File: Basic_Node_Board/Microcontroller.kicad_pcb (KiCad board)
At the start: 4 copper layers, 100 x 100 mm, 31 parts, among them J1 Conn_01x02, J4 Conn_01x02_Pin, U2 ESP32-DEVKIT-C, U3 TPS54560BQDDARQ1, U6 TJA1050T/CM,118

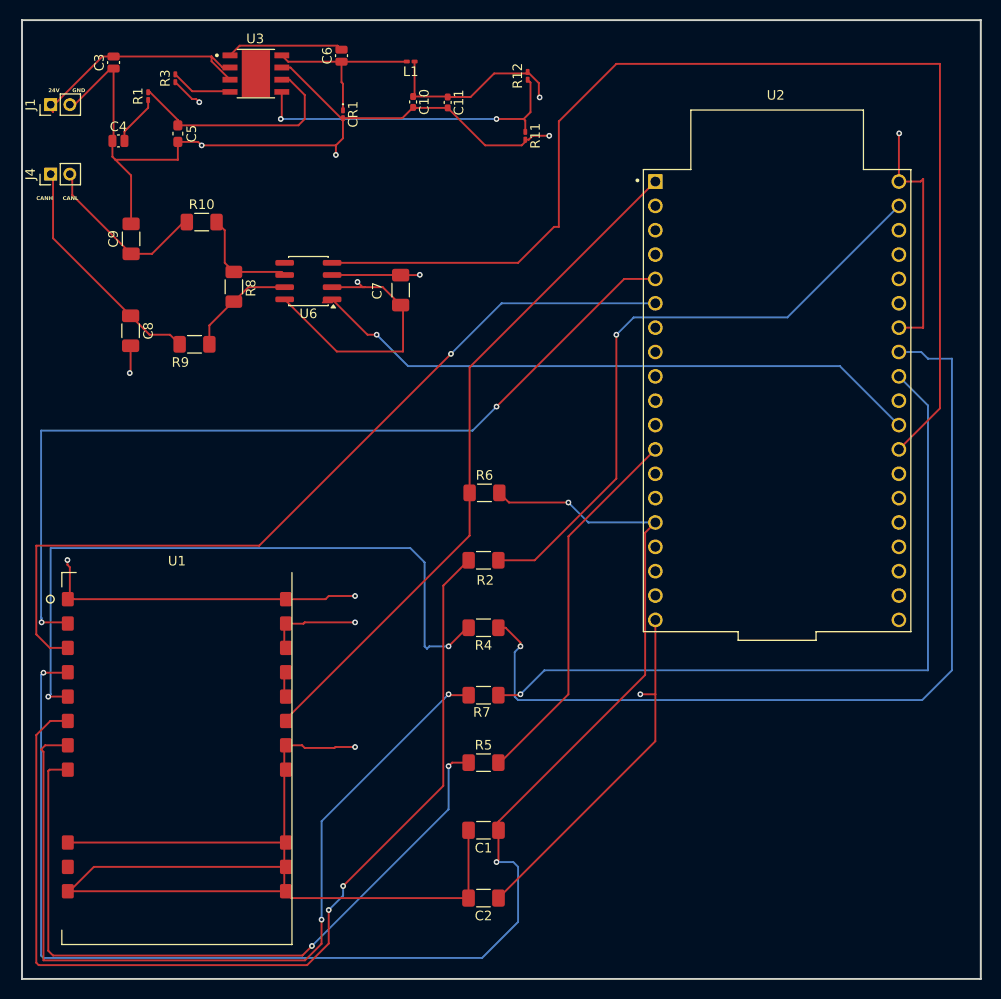
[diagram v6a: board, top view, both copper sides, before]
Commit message: verified all componnents are 1206 for SMD
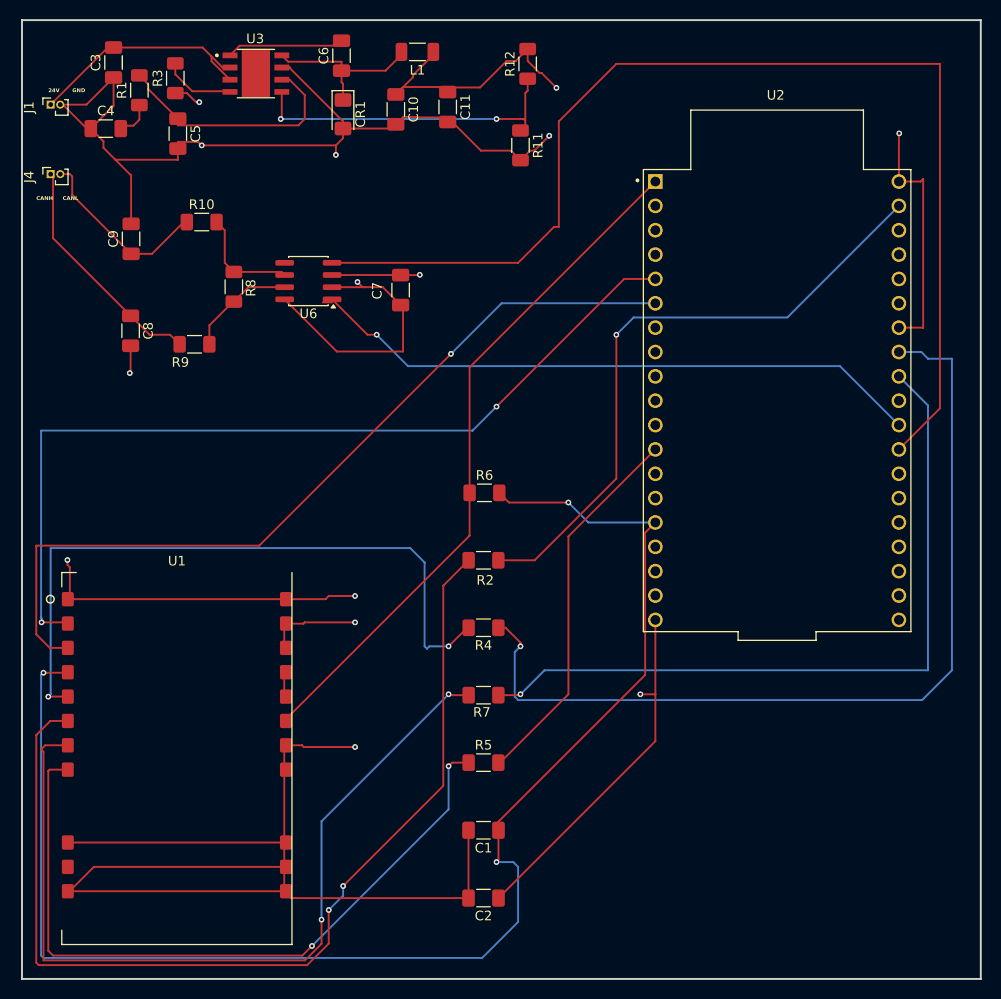
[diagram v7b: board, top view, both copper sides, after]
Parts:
- C10, C11: footprint Capacitor_SMD:C_0402_1005Metric_Pad0.74x0.62mm_HandSolder -> Capacitor_SMD:C_1206_3216Metric_Pad1.33x1.80mm_HandSolder
- C3, C4: footprint Capacitor_SMD:C_0504_1310Metric_Pad0.83x1.28mm_HandSolder -> Capacitor_SMD:C_1206_3216Metric_Pad1.33x1.80mm_HandSolder
- C5: footprint Capacitor_SMD:C_0603_1608Metric_Pad1.08x0.95mm_HandSolder -> Capacitor_SMD:C_1206_3216Metric_Pad1.33x1.80mm_HandSolder
- C6: value 08053C104KAT2A -> 100nF; footprint Capacitor_SMD:C_0504_1310Metric_Pad0.83x1.28mm_HandSolder -> Capacitor_SMD:C_1206_3216Metric_Pad1.33x1.80mm_HandSolder
- CR1: value B560C-13-F -> SS34; footprint Diode_SMD:D_0201_0603Metric_Pad0.64x0.40mm_HandSolder -> Diode_SMD:D_1206_3216Metric_Pad1.42x1.75mm_HandSolder
- J1, J4: footprint Connector_PinHeader_2.00mm:PinHeader_1x02_P2.00mm_Vertical -> Connector_PinSocket_1.00mm:PinSocket_1x02_P1.00mm_Vertical
- L1: footprint Inductor_SMD:L_0201_0603Metric_Pad0.64x0.40mm_HandSolder -> Inductor_SMD:L_1206_3216Metric_Pad1.22x1.90mm_HandSolder
- R1, R11, R12, R3: footprint Resistor_SMD:R_0201_0603Metric_Pad0.64x0.40mm_HandSolder -> Resistor_SMD:R_1206_3216Metric_Pad1.30x1.75mm_HandSolder
- moved C10 1.96 mm to (74.5, 34.0)
- moved C4 1.84 mm to (44.2, 36.0)
- moved R12 1.25 mm to (88.2, 29.2)
- moved L1 1.23 mm to (76.8, 28.0)
- moved R11 1.12 mm to (87.5, 37.8)
- moved R1 1.10 mm to (47.8, 32.0)
- moved C11 0.48 mm to (79.9, 33.8)
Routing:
- net 5.3V OUT: track 180.8 -> 190.5 mm
- net GND: track 463.1 -> 468.5 mm
- net Net-(U3-COMP): track 23.9 -> 25.8 mm
- net Net-(C4-Pad2): track 5.29 -> 3.85 mm
- net Net-(U3-RT/CLK): track 6.46 -> 7.60 mm
- net /CANL: track 18.1 -> 19.1 mm
- net Net-(U3-SW): track 18.5 -> 17.8 mm
- net /24V: track 26.2 -> 25.6 mm
- net Net-(U3-BOOT): track 12.2 -> 11.6 mm

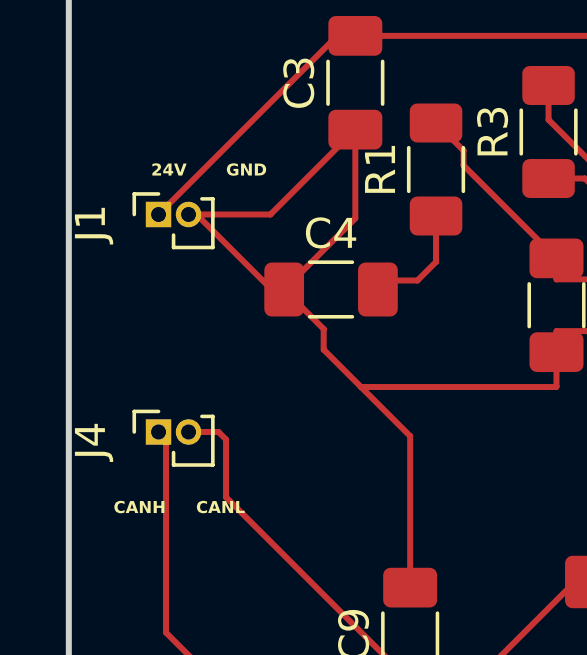
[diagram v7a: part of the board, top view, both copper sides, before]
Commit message: reverified pin headers for canbus and power
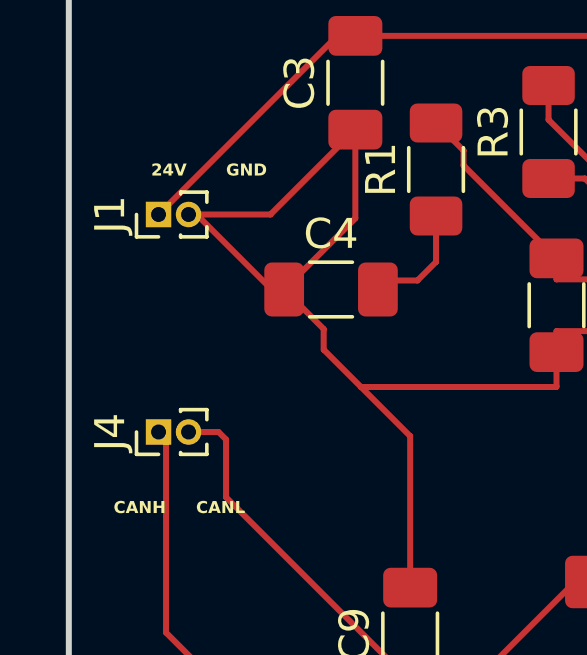
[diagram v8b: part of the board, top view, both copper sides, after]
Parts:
- J1, J4: footprint Connector_PinSocket_1.00mm:PinSocket_1x02_P1.00mm_Vertical -> Connector_PinHeader_1.00mm:PinHeader_1x02_P1.00mm_Vertical
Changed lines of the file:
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@@
 		)
 	)
-	(footprint "Connector_PinSocket_1.00mm:PinSocket_1x02_P1.00mm_Vertical"
+	(footprint "Connector_PinHeader_1.00mm:PinHeader_1x02_P1.00mm_Vertical"
 		(layer "F.Cu")
 		(at 38.5 40.75 90)
-		(descr "Through hole straight socket strip, 1x02, 1.00mm pitch, single row (https://gct.co/files/drawings/bc065.pdf), script generated")
-		(tags "Through hole socket strip THT 1x02 1.00mm single row")
+		(descr "Through hole straight pin header, 1x02, 1.00mm pitch, single row")
+		(tags "Through hole pin header THT 1x02 1.00mm single row")
 		(property "Reference" "J4"
-			(at -0.29 -2.25 90)
+			(at 0 -1.61 90)
 			(layer "F.SilkS")
 			(effects
@@
 		)
 		(property "Value" "Conn_01x02_Pin"
-			(at -0.29 3.25 90)
+			(at 0 2.61 90)
 			(layer "F.Fab")
 			(effects
@@
 		(attr through_hole)
 		(fp_line
-			(start 0.685 -0.81)
-			(end 0.685 0)
+			(start -0.745 -0.735)
+			(end 0 -0.735)
 			(stroke
 				(width 0.12)
@@
 		)
 		(fp_line
-			(start 0 -0.81)
-			(end 0.685 -0.81)
+			(start -0.745 0)
+			(end -0.745 -0.735)
 			(stroke
 				(width 0.12)
@@
 		)
 		(fp_line
-			(start -1.1 0.5)
-			(end -0.685 0.5)
+			(start 0.745 0.735)
+			(end 0.745 1.61)
 			(stroke
 				(width 0.12)
@@
 		)
 		(fp_line
-			(start -1.1 0.5)
-			(end -1.1 1.81)
+			(start 0.685565 0.735)
+			(end 0.745 0.735)
 			(stroke
 				(width 0.12)
@@
 		)
 		(fp_line
-			(start 0.52 1.445898)
-			(end 0.52 1.81)
+			(start -0.745 0.735)
+			(end -0.685565 0.735)
 			(stroke
 				(width 0.12)
@@
 		)
 		(fp_line
-			(start -1.1 1.81)
-			(end 0.52 1.81)
+			(start -0.745 0.735)
+			(end -0.745 1.61)
 			(stroke
 				(width 0.12)
@@
 		)
 		(fp_line
-			(start 0.96 -1.25)
-			(end 0.96 2.25)
+			(start 0.41003 1.61)
+			(end 0.745 1.61)
 			(stroke
-				(width 0.05)
-				(type solid)
-			)
-			(layer "F.CrtYd")
-		)
-		(fp_line
-			(start -1.54 -1.25)
-			(end 0.96 -1.25)
-			(stroke
-				(width 0.05)
+				(width 0.12)
 				(type solid)
 			)
-			(layer "F.CrtYd")
+			(layer "F.SilkS")
 		)
 		(fp_line
-			(start 0.96 2.25)
-			(end -1.54 2.25)
+			(start -0.745 1.61)
+			(end -0.41003 1.61)
 			(stroke
-				(width 0.05)
+				(width 0.12)
 				(type solid)
 			)
-			(layer "F.CrtYd")
+			(layer "F.SilkS")
 		)
-		(fp_line
-			(start -1.54 2.25)
-			(end -1.54 -1.25)
+		(fp_rect
+			(start -1.14 -1)
+			(end 1.14 2)
 			(stroke
 				(width 0.05)
 				(type solid)
 			)
+			(fill no)
 			(layer "F.CrtYd")
 		)
 		(fp_line
-			(start 0.085 -0.75)
-			(end 0.46 -0.375)
+			(start 0.635 -0.5)
+			(end 0.635 1.5)
 			(stroke
 				(width 0.1)
@@
 		)
 		(fp_line
-			(start -1.04 -0.75)
-			(end 0.085 -0.75)
+			(start -0.3175 -0.5)
+			(end 0.635 -0.5)
 			(stroke
 				(width 0.1)
@@
 		)
 		(fp_line
-			(start 0.46 -0.375)
-			(end 0.46 1.75)
+			(start -0.635 -0.1825)
+			(end -0.3175 -0.5)
 			(stroke
 				(width 0.1)
@@
 		)
 		(fp_line
-			(start 0.46 1.75)
-			(end -1.04 1.75)
+			(start 0.635 1.5)
+			(end -0.635 1.5)
 			(stroke
 				(width 0.1)
@@
 		)
 		(fp_line
-			(start -1.04 1.75)
-			(end -1.04 -0.75)
+			(start -0.635 1.5)
+			(end -0.635 -0.1825)
 			(stroke
 				(width 0.1)
@@
 		)
 		(fp_text user "${REFERENCE}"
-			(at -0.29 0.5 180)
+			(at 0 0.5 180)
 			(layer "F.Fab")
 			(effects
 				(font
-					(size 0.9 0.9)
-					(thickness 0.14)
+					(size 0.76 0.76)
+					(thickness 0.114)
 				)
 			)
@@
 		)
 		(embedded_fonts no)
-		(model "${KICAD9_3DMODEL_DIR}/Connector_PinSocket_1.00mm.3dshapes/PinSocket_1x02_P1.00mm_Vertical.step"
+		(model "${KICAD9_3DMODEL_DIR}/Connector_PinHeader_1.00mm.3dshapes/PinHeader_1x02_P1.00mm_Vertical.step"
 			(offset
 				(xyz 0 0 0)
@@
 		)
 	)
-	(footprint "Connector_PinSocket_1.00mm:PinSocket_1x02_P1.00mm_Vertical"
+	(footprint "Connector_PinHeader_1.00mm:PinHeader_1x02_P1.00mm_Vertical"
 		(layer "F.Cu")
 		(at 38.5 33.5 90)
-		(descr "Through hole straight socket strip, 1x02, 1.00mm pitch, single row (https://gct.co/files/drawings/bc065.pdf), script generated")
-		(tags "Through hole socket strip THT 1x02 1.00mm single row")
+		(descr "Through hole straight pin header, 1x02, 1.00mm pitch, single row")
+		(tags "Through hole pin header THT 1x02 1.00mm single row")
 		(property "Reference" "J1"
-			(at -0.29 -2.25 90)
+			(at 0 -1.61 90)
 			(layer "F.SilkS")
 			(effects
@@
 		)
 		(property "Value" "Conn_01x02"
-			(at -0.29 3.25 90)
+			(at 0 2.61 90)
 			(layer "F.Fab")
 			(effects
@@
 		(attr through_hole)
 		(fp_line
-			(start 0.685 -0.81)
-			(end 0.685 0)
+			(start -0.745 -0.735)
+			(end 0 -0.735)
 			(stroke
 				(width 0.12)
@@
 		)
 		(fp_line
-			(start 0 -0.81)
-			(end 0.685 -0.81)
+			(start -0.745 0)
+			(end -0.745 -0.735)
 			(stroke
 				(width 0.12)
@@
 		)
 		(fp_line
-			(start -1.1 0.5)
-			(end -0.685 0.5)
+			(start 0.745 0.735)
+			(end 0.745 1.61)
 			(stroke
 				(width 0.12)
@@
 		)
 		(fp_line
-			(start -1.1 0.5)
-			(end -1.1 1.81)
+			(start 0.685565 0.735)
+			(end 0.745 0.735)
 			(stroke
 				(width 0.12)
@@
 		)
 		(fp_line
-			(start 0.52 1.445898)
-			(end 0.52 1.81)
+			(start -0.745 0.735)
+			(end -0.685565 0.735)
 			(stroke
 				(width 0.12)
@@
 		)
 		(fp_line
-			(start -1.1 1.81)
-			(end 0.52 1.81)
+			(start -0.745 0.735)
+			(end -0.745 1.61)
 			(stroke
 				(width 0.12)
@@
 		)
 		(fp_line
-			(start 0.96 -1.25)
-			(end 0.96 2.25)
+			(start 0.41003 1.61)
+			(end 0.745 1.61)
 			(stroke
-				(width 0.05)
-				(type solid)
-			)
-			(layer "F.CrtYd")
-		)
-		(fp_line
-			(start -1.54 -1.25)
-			(end 0.96 -1.25)
-			(stroke
-				(width 0.05)
+				(width 0.12)
 				(type solid)
 			)
-			(layer "F.CrtYd")
+			(layer "F.SilkS")
 		)
 		(fp_line
-			(start 0.96 2.25)
-			(end -1.54 2.25)
+			(start -0.745 1.61)
+			(end -0.41003 1.61)
 			(stroke
-				(width 0.05)
+				(width 0.12)
 				(type solid)
 			)
-			(layer "F.CrtYd")
+			(layer "F.SilkS")
 		)
-		(fp_line
-			(start -1.54 2.25)
-			(end -1.54 -1.25)
+		(fp_rect
+			(start -1.14 -1)
+			(end 1.14 2)
 			(stroke
 				(width 0.05)
 				(type solid)
 			)
+			(fill no)
 			(layer "F.CrtYd")
 		)
 		(fp_line
-			(start 0.085 -0.75)
-			(end 0.46 -0.375)
+			(start 0.635 -0.5)
+			(end 0.635 1.5)
 			(stroke
 				(width 0.1)
@@
 		)
 		(fp_line
-			(start -1.04 -0.75)
-			(end 0.085 -0.75)
+			(start -0.3175 -0.5)
+			(end 0.635 -0.5)
 			(stroke
 				(width 0.1)
@@
 		)
 		(fp_line
-			(start 0.46 -0.375)
-			(end 0.46 1.75)
+			(start -0.635 -0.1825)
+			(end -0.3175 -0.5)
 			(stroke
 				(width 0.1)
@@
 		)
 		(fp_line
-			(start 0.46 1.75)
-			(end -1.04 1.75)
+			(start 0.635 1.5)
+			(end -0.635 1.5)
 			(stroke
 				(width 0.1)
@@
 		)
 		(fp_line
-			(start -1.04 1.75)
-			(end -1.04 -0.75)
+			(start -0.635 1.5)
+			(end -0.635 -0.1825)
 			(stroke
 				(width 0.1)
@@
 		)
 		(fp_text user "${REFERENCE}"
-			(at -0.29 0.5 180)
+			(at 0 0.5 180)
 			(layer "F.Fab")
 			(effects
 				(font
-					(size 0.9 0.9)
-					(thickness 0.14)
+					(size 0.76 0.76)
+					(thickness 0.114)
 				)
 			)
@@
 		)
 		(embedded_fonts no)
-		(model "${KICAD9_3DMODEL_DIR}/Connector_PinSocket_1.00mm.3dshapes/PinSocket_1x02_P1.00mm_Vertical.step"
+		(model "${KICAD9_3DMODEL_DIR}/Connector_PinHeader_1.00mm.3dshapes/PinHeader_1x02_P1.00mm_Vertical.step"
 			(offset
 				(xyz 0 0 0)
